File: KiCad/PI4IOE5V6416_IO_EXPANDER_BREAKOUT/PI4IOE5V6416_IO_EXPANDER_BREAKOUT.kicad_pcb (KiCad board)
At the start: 2 copper layers, 22.9 x 33 mm, 15 parts, among them J1 Conn_01x12_Pin, J2 Conn_01x12_Pin, U2 LP5907MFX-3.3, U3 PI4IOE5V6416-TQFN

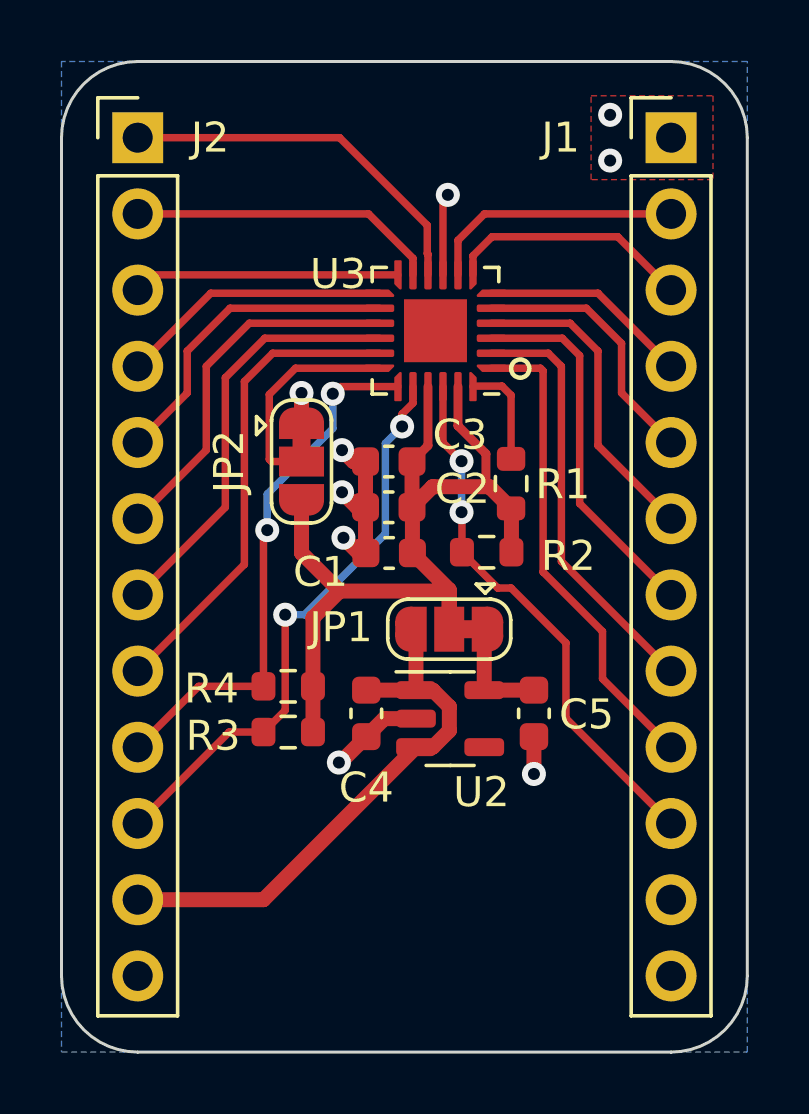
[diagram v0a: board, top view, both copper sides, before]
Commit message: Revision 4
- Remove unnecessary pin headers
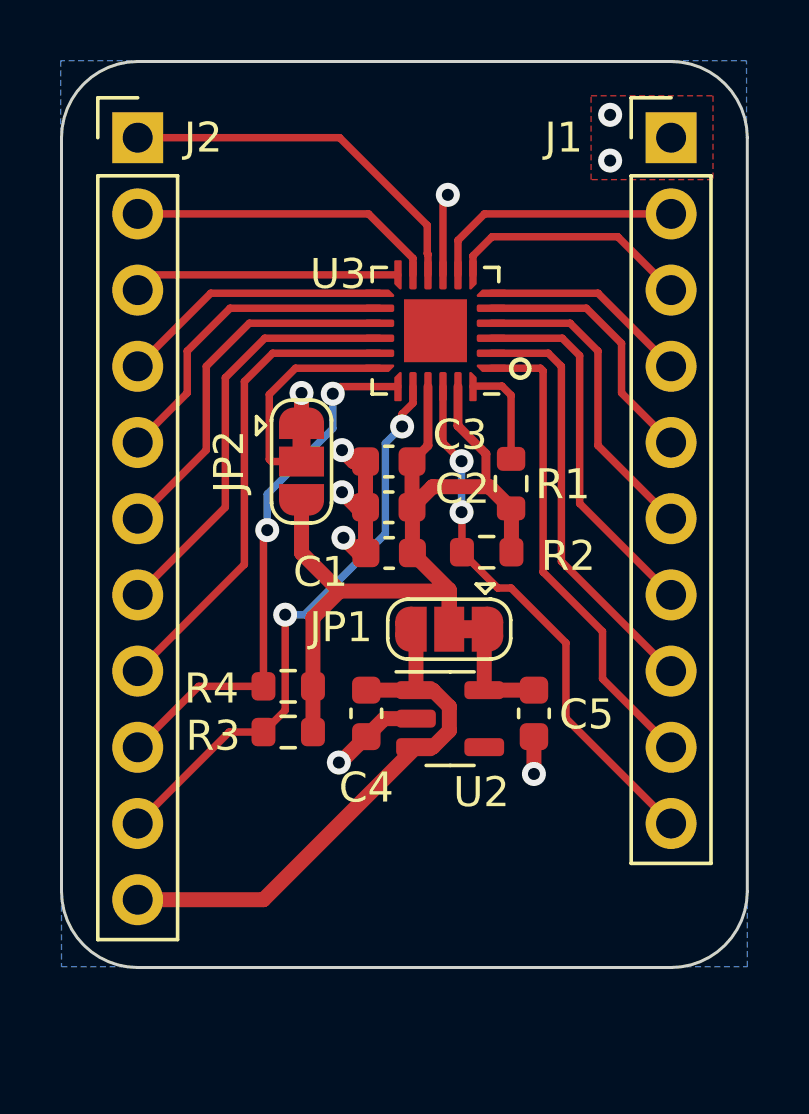
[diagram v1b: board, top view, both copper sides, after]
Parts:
- J1: value Conn_01x12_Pin -> Conn_01x10_Pin; footprint Connector_PinHeader_2.54mm:PinHeader_1x12_P2.54mm_Vertical -> Connector_PinHeader_2.54mm:PinHeader_1x10_P2.54mm_Vertical
- J2: value Conn_01x12_Pin -> Conn_01x11_Pin; footprint Connector_PinHeader_2.54mm:PinHeader_1x12_P2.54mm_Vertical -> Connector_PinHeader_2.54mm:PinHeader_1x11_P2.54mm_Vertical
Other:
- board size 22.9 x 33 mm -> 22.9 x 30.2 mm
- board text removed: "NC"
